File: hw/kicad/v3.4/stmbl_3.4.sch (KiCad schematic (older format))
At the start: 2 parts

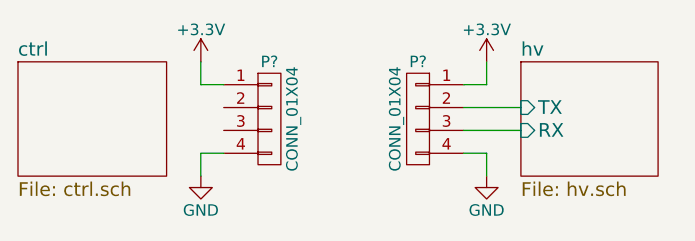
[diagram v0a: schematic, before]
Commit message: gitignore kicad bak files, hv tx fix
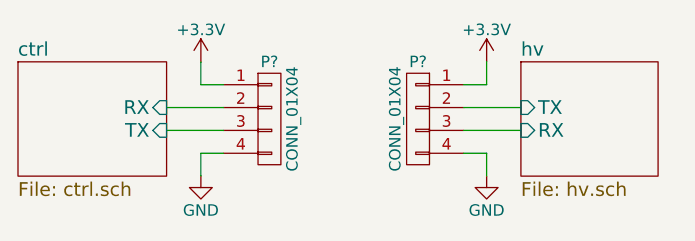
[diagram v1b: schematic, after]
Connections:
- net ctrl/RX: now reaches P?.2 (P2)
- net ctrl/TX: now reaches P?.3 (P3)
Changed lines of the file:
@@
 EESchema Schematic File Version 2
+LIBS:power
 LIBS:stmbl_3.4-cache
 EELAYER 25 0
@@
 F0 "ctrl" 60
 F1 "ctrl.sch" 60
+F2 "TX" I R 4950 2600 60
+F3 "RX" I R 4950 2500 60
 $EndSheet
 $Comp
@@
 Wire Wire Line
 	5100 2700 5100 2800
+Wire Wire Line
+	4950 2500 5200 2500
+Wire Wire Line
+	4950 2600 5200 2600
 $EndSCHEMATC
